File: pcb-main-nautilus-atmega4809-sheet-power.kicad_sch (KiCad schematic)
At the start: 14 parts, among them U1 NCP1117-5.0_TO252, U2 AP2112K-3.3

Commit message: Switch to generated Digi-Key and Mouser links
Supports #2.
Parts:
- C1: Digi-Key https://www.digikey.com/en/products/detail/panasonic-electr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 -> (none); Digi-Key Part Number (none) -> PCE3753CT-ND; Mouser https://www.mouser.com/ProductDetail/Panasonic/EEE-HC1E470X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 -> (none); Mouser Part Number (none) -> 667-EEE-HC1E470XP
- C2: Digi-Key https://www.digikey.com/en/products/detail/kemet/C0603C104M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 -> (none); Digi-Key Part Number (none) -> 399-C0603C104M3RAC7867CT-ND; Mouser https://www.mouser.com/ProductDetail/KEMET/C0603C104M3RAC?q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 -> (none); Mouser Part Number (none) -> 80-C0603C104M3RAC
- C3: Digi-Key https://www.digikey.com/en/products/detail/panasonic-electr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 -> (none); Digi-Key Part Number (none) -> 10-EEE-FN1A470URCT-ND; Mouser https://www.mouser.com/ProductDetail/Panasonic/EEE-FN1A470U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 -> (none); Mouser Part Number (none) -> 667-EEE-FN1A470UR
- C4, C6: Digi-Key https://www.digikey.com/en/products/detail/kemet/C0603C104M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 -> (none); Digi-Key Part Number (none) -> 399-C0603C104M8RAC7867CT-ND; Mouser https://www.mouser.com/ProductDetail/KEMET/C0603C104M8RACTU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 -> (none); Mouser Part Number (none) -> 80-C0603C104M8R
- C5: Digi-Key https://www.digikey.com/en/products/detail/kemet/C0603C106M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 -> (none); Digi-Key Part Number (none) -> 399-C0603C106M9PAC7867CT-ND; Mouser https://www.mouser.com/ProductDetail/KEMET/C0603C106M9PAC?q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 -> (none); Mouser Part Number (none) -> 80-C0603C106M9PAC
- D1, D2: Digi-Key https://www.digikey.com/en/products/detail/onsemi/MBR120LSF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 -> (none); Digi-Key Part Number (none) -> MBR120LSFT3GOSCT-ND; Mouser https://www.mouser.com/ProductDetail/onsemi/MBR120LSFT3G?qs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 -> (none); Mouser Part Number (none) -> 863-MBR120LSFT3G
- D3, D4: Digi-Key https://www.digikey.com/en/products/detail/liteon/LTST-C190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 -> (none); Digi-Key Part Number (none) -> 160-1435-1-ND; Mouser https://www.mouser.com/ProductDetail/Lite-On/LTST-C190KGKT?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 -> (none); Mouser Part Number (none) -> 859-LTST-C190KGKT
- R1, R2: Digi-Key https://www.digikey.com/en/products/detail/panasonic-electr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 -> (none); Digi-Key Part Number (none) -> P330HCT-ND; Mouser https://www.mouser.com/ProductDetail/Panasonic/ERJ-3EKF3300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 -> (none); Mouser Part Number (none) -> 667-ERJ-3EKF3300V
- U1: Digi-Key https://www.digikey.com/en/products/detail/onsemi/NCP1117DT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 -> (none); Digi-Key Part Number (none) -> NCP1117DT50RKGOSCT-ND; Mouser https://www.mouser.com/ProductDetail/onsemi/NCP1117DT50RKG?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 -> (none); Mouser Part Number (none) -> 863-NCP1117DT50RKG
- U2: Digi-Key https://www.digikey.com/en/products/detail/diodes-incorpora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 -> (none); Digi-Key Part Number (none) -> AP2112K-3.3TRG1DICT-ND; Mouser https://www.mouser.com/ProductDetail/Diodes-Incorporated/AP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 -> (none); Mouser Part Number (none) -> 621-AP2112K-3.3TRG1
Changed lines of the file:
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@@
       (effects (font (size 1.27 1.27)) hide)
     )
-    (property "Digi-Key" "https://www.digikey.com/en/products/detail/liteon/LTST-C190KGKT/386815" (id 6) (at 196.85 74.93 90)
-      (effects (font (size 1.27 1.27)) hide)
-    )
-    (property "Mouser" "https://www.mouser.com/ProductDetail/Lite-On/LTST-C190KGKT?qs=205qCy6M2Q%252BAdcgwUZktqw%3D%3D" (id 7) (at 196.85 74.93 90)
+    (property "Digi-Key Part Number" "160-1435-1-ND" (id 6) (at 196.85 74.93 90)
+      (effects (font (size 1.27 1.27)) hide)
+    )
+    (property "Mouser Part Number" "859-LTST-C190KGKT" (id 7) (at 196.85 74.93 90)
       (effects (font (size 1.27 1.27)) hide)
     )
@@
       (effects (font (size 1.27 1.27)) hide)
     )
-    (property "Digi-Key" "https://www.digikey.com/en/products/detail/panasonic-electronic-components/ERJ-3EKF3300V/1746374" (id 6) (at 196.85 85.09 0)
-      (effects (font (size 1.27 1.27)) hide)
-    )
-    (property "Mouser" "https://www.mouser.com/ProductDetail/Panasonic/ERJ-3EKF3300V?qs=MVjVSMjNRMqskx0rzM4%2FYg%3D%3D" (id 7) (at 196.85 85.09 0)
+    (property "Digi-Key Part Number" "P330HCT-ND" (id 6) (at 196.85 85.09 0)
+      (effects (font (size 1.27 1.27)) hide)
+    )
+    (property "Mouser Part Number" "667-ERJ-3EKF3300V" (id 7) (at 196.85 85.09 0)
       (effects (font (size 1.27 1.27)) hide)
     )
@@
       (effects (font (size 1.27 1.27)) hide)
     )
-    (property "Digi-Key" "https://www.digikey.com/en/products/detail/kemet/C0603C104M8RAC7867/2199783" (id 6) (at 177.8 135.89 0)
-      (effects (font (size 1.27 1.27)) hide)
-    )
-    (property "Mouser" "https://www.mouser.com/ProductDetail/KEMET/C0603C104M8RACTU?qs=t9q%2F2xDdjt%252BO6KYorkYlEw%3D%3D" (id 7) (at 177.8 135.89 0)
+    (property "Digi-Key Part Number" "399-C0603C104M8RAC7867CT-ND" (id 6) (at 177.8 135.89 0)
+      (effects (font (size 1.27 1.27)) hide)
+    )
+    (property "Mouser Part Number" "80-C0603C104M8R" (id 7) (at 177.8 135.89 0)
       (effects (font (size 1.27 1.27)) hide)
     )
@@
       (effects (font (size 1.27 1.27)) hide)
     )
-    (property "Digi-Key" "https://www.digikey.com/en/products/detail/onsemi/NCP1117DT50RKG/661206" (id 6) (at 139.7 69.85 0)
-      (effects (font (size 1.27 1.27)) hide)
-    )
-    (property "Mouser" "https://www.mouser.com/ProductDetail/onsemi/NCP1117DT50RKG?qs=Gev%252BmEvV0iaGLyZQ1w6kFw%3D%3D" (id 7) (at 139.7 69.85 0)
+    (property "Digi-Key Part Number" "NCP1117DT50RKGOSCT-ND" (id 6) (at 139.7 69.85 0)
+      (effects (font (size 1.27 1.27)) hide)
+    )
+    (property "Mouser Part Number" "863-NCP1117DT50RKG" (id 7) (at 139.7 69.85 0)
       (effects (font (size 1.27 1.27)) hide)
     )
@@
       (effects (font (size 1.27 1.27)) hide)
     )
-    (property "Digi-Key" "https://www.digikey.com/en/products/detail/panasonic-electronic-components/EEE-HC1E470XP/672769" (id 6) (at 101.6 74.93 0)
-      (effects (font (size 1.27 1.27)) hide)
-    )
-    (property "Mouser" "https://www.mouser.com/ProductDetail/Panasonic/EEE-HC1E470XP?qs=Ywefl8B65e6qyZdKUyDlkQ%3D%3D" (id 7) (at 101.6 74.93 0)
+    (property "Digi-Key Part Number" "PCE3753CT-ND" (id 6) (at 101.6 74.93 0)
+      (effects (font (size 1.27 1.27)) hide)
+    )
+    (property "Mouser Part Number" "667-EEE-HC1E470XP" (id 7) (at 101.6 74.93 0)
       (effects (font (size 1.27 1.27)) hide)
     )
@@
       (effects (font (size 1.27 1.27)) hide)
     )
-    (property "Digi-Key" "https://www.digikey.com/en/products/detail/onsemi/MBR120LSFT3G/1477155" (id 6) (at 82.55 64.77 0)
-      (effects (font (size 1.27 1.27)) hide)
-    )
-    (property "Mouser" "https://www.mouser.com/ProductDetail/onsemi/MBR120LSFT3G?qs=3JMERSakebrl0QzFyBgvHg%3D%3D" (id 7) (at 82.55 64.77 0)
+    (property "Digi-Key Part Number" "MBR120LSFT3GOSCT-ND" (id 6) (at 82.55 64.77 0)
+      (effects (font (size 1.27 1.27)) hide)
+    )
+    (property "Mouser Part Number" "863-MBR120LSFT3G" (id 7) (at 82.55 64.77 0)
       (effects (font (size 1.27 1.27)) hide)
     )
@@
       (effects (font (size 1.27 1.27)) hide)
     )
-    (property "Digi-Key" "https://www.digikey.com/en/products/detail/panasonic-electronic-components/EEE-FN1A470UR/11656979" (id 6) (at 158.75 74.93 0)
-      (effects (font (size 1.27 1.27)) hide)
-    )
-    (property "Mouser" "https://www.mouser.com/ProductDetail/Panasonic/EEE-FN1A470UR?qs=OlC7AqGiEDlZjloUmme03Q%3D%3D" (id 7) (at 158.75 74.93 0)
+    (property "Digi-Key Part Number" "10-EEE-FN1A470URCT-ND" (id 6) (at 158.75 74.93 0)
+      (effects (font (size 1.27 1.27)) hide)
+    )
+    (property "Mouser Part Number" "667-EEE-FN1A470UR" (id 7) (at 158.75 74.93 0)
       (effects (font (size 1.27 1.27)) hide)
     )
@@
       (effects (font (size 1.27 1.27)) hide)
     )
-    (property "Digi-Key" "https://www.digikey.com/en/products/detail/kemet/C0603C104M8RAC7867/2199783" (id 6) (at 177.8 74.93 0)
-      (effects (font (size 1.27 1.27)) hide)
-    )
-    (property "Mouser" "https://www.mouser.com/ProductDetail/KEMET/C0603C104M8RACTU?qs=t9q%2F2xDdjt%252BO6KYorkYlEw%3D%3D" (id 7) (at 177.8 74.93 0)
+    (property "Digi-Key Part Number" "399-C0603C104M8RAC7867CT-ND" (id 6) (at 177.8 74.93 0)
+      (effects (font (size 1.27 1.27)) hide)
+    )
+    (property "Mouser Part Number" "80-C0603C104M8R" (id 7) (at 177.8 74.93 0)
       (effects (font (size 1.27 1.27)) hide)
     )
@@
       (effects (font (size 1.27 1.27)) hide)
     )
-    (property "Digi-Key" "https://www.digikey.com/en/products/detail/liteon/LTST-C190KGKT/386815" (id 6) (at 196.85 135.89 90)
-      (effects (font (size 1.27 1.27)) hide)
-    )
-    (property "Mouser" "https://www.mouser.com/ProductDetail/Lite-On/LTST-C190KGKT?qs=205qCy6M2Q%252BAdcgwUZktqw%3D%3D" (id 7) (at 196.85 135.89 90)
+    (property "Digi-Key Part Number" "160-1435-1-ND" (id 6) (at 196.85 135.89 90)
+      (effects (font (size 1.27 1.27)) hide)
+    )
+    (property "Mouser Part Number" "859-LTST-C190KGKT" (id 7) (at 196.85 135.89 90)
       (effects (font (size 1.27 1.27)) hide)
     )
@@
       (effects (font (size 1.27 1.27)) hide)
     )
-    (property "Digi-Key" "https://www.digikey.com/en/products/detail/kemet/C0603C104M3RAC7867/416046" (id 6) (at 120.65 74.93 0)
-      (effects (font (size 1.27 1.27)) hide)
-    )
-    (property "Mouser" "https://www.mouser.com/ProductDetail/KEMET/C0603C104M3RAC?qs=zlI8QACJnq99iivvUDrLjA%3D%3D" (id 7) (at 120.65 74.93 0)
+    (property "Digi-Key Part Number" "399-C0603C104M3RAC7867CT-ND" (id 6) (at 120.65 74.93 0)
+      (effects (font (size 1.27 1.27)) hide)
+    )
+    (property "Mouser Part Number" "80-C0603C104M3RAC" (id 7) (at 120.65 74.93 0)
       (effects (font (size 1.27 1.27)) hide)
     )
@@
       (effects (font (size 1.27 1.27)) hide)
     )
-    (property "Digi-Key" "https://www.digikey.com/en/products/detail/onsemi/MBR120LSFT3G/1477155" (id 6) (at 153.67 64.77 0)
-      (effects (font (size 1.27 1.27)) hide)
-    )
-    (property "Mouser" "https://www.mouser.com/ProductDetail/onsemi/MBR120LSFT3G?qs=3JMERSakebrl0QzFyBgvHg%3D%3D" (id 7) (at 153.67 64.77 0)
+    (property "Digi-Key Part Number" "MBR120LSFT3GOSCT-ND" (id 6) (at 153.67 64.77 0)
+      (effects (font (size 1.27 1.27)) hide)
+    )
+    (property "Mouser Part Number" "863-MBR120LSFT3G" (id 7) (at 153.67 64.77 0)
       (effects (font (size 1.27 1.27)) hide)
     )
@@
       (effects (font (size 1.27 1.27)) hide)
     )
-    (property "Digi-Key" "https://www.digikey.com/en/products/detail/panasonic-electronic-components/ERJ-3EKF3300V/1746374" (id 6) (at 196.85 146.05 0)
-      (effects (font (size 1.27 1.27)) hide)
-    )
-    (property "Mouser" "https://www.mouser.com/ProductDetail/Panasonic/ERJ-3EKF3300V?qs=MVjVSMjNRMqskx0rzM4%2FYg%3D%3D" (id 7) (at 196.85 146.05 0)
+    (property "Digi-Key Part Number" "P330HCT-ND" (id 6) (at 196.85 146.05 0)
+      (effects (font (size 1.27 1.27)) hide)
+    )
+    (property "Mouser Part Number" "667-ERJ-3EKF3300V" (id 7) (at 196.85 146.05 0)
       (effects (font (size 1.27 1.27)) hide)
     )
@@
       (effects (font (size 1.27 1.27)) hide)
     )
-    (property "Digi-Key" "https://www.digikey.com/en/products/detail/kemet/C0603C106M9PAC7867/1950664" (id 6) (at 158.75 135.89 0)
-      (effects (font (size 1.27 1.27)) hide)
-    )
-    (property "Mouser" "https://www.mouser.com/ProductDetail/KEMET/C0603C106M9PAC?qs=vnwGVgFuQibgQzzOtLArWQ%3D%3D" (id 7) (at 158.75 135.89 0)
+    (property "Digi-Key Part Number" "399-C0603C106M9PAC7867CT-ND" (id 6) (at 158.75 135.89 0)
+      (effects (font (size 1.27 1.27)) hide)
+    )
+    (property "Mouser Part Number" "80-C0603C106M9PAC" (id 7) (at 158.75 135.89 0)
       (effects (font (size 1.27 1.27)) hide)
     )
@@
       (effects (font (size 1.27 1.27)) hide)
     )
-    (property "Digi-Key" "https://www.digikey.com/en/products/detail/diodes-incorporated/AP2112K-3-3TRG1/4470746" (id 6) (at 139.7 133.35 0)
-      (effects (font (size 1.27 1.27)) hide)
-    )
-    (property "Mouser" "https://www.mouser.com/ProductDetail/Diodes-Incorporated/AP2112K-3.3TRG1?qs=x6A8l6qLYDDPYHosCdzh%2FA%3D%3D" (id 7) (at 139.7 133.35 0)
-      (effects (font (size 1.27 1.27)) hide)
-    )
+    (property "Digi-Key Part Number" "AP2112K-3.3TRG1DICT-ND" (id 6) (at 139.7 133.35 0)
+      (effects (font (size 1.27 1.27)) hide)
+    )
+    (property "Mouser Part Number" "621-AP2112K-3.3TRG1" (id 7) (at 139.7 133.35 0)
+      (effects (font (size 1.27 1.27)) hide)
+    )

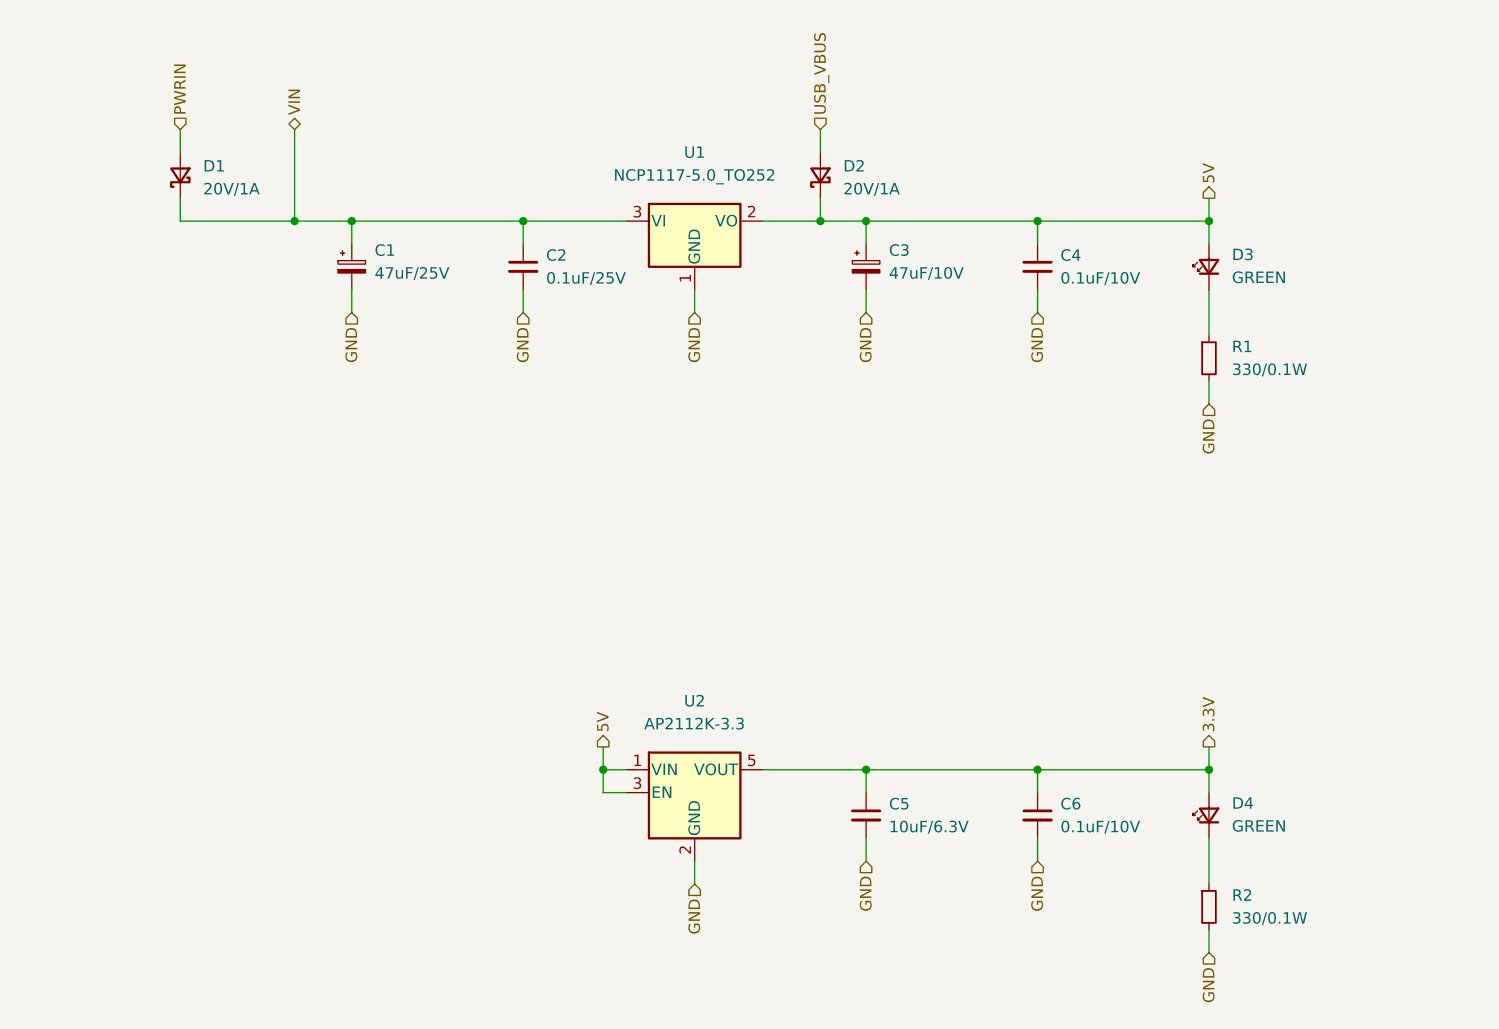
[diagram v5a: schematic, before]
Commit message: Connect root sheet
Supports #2.
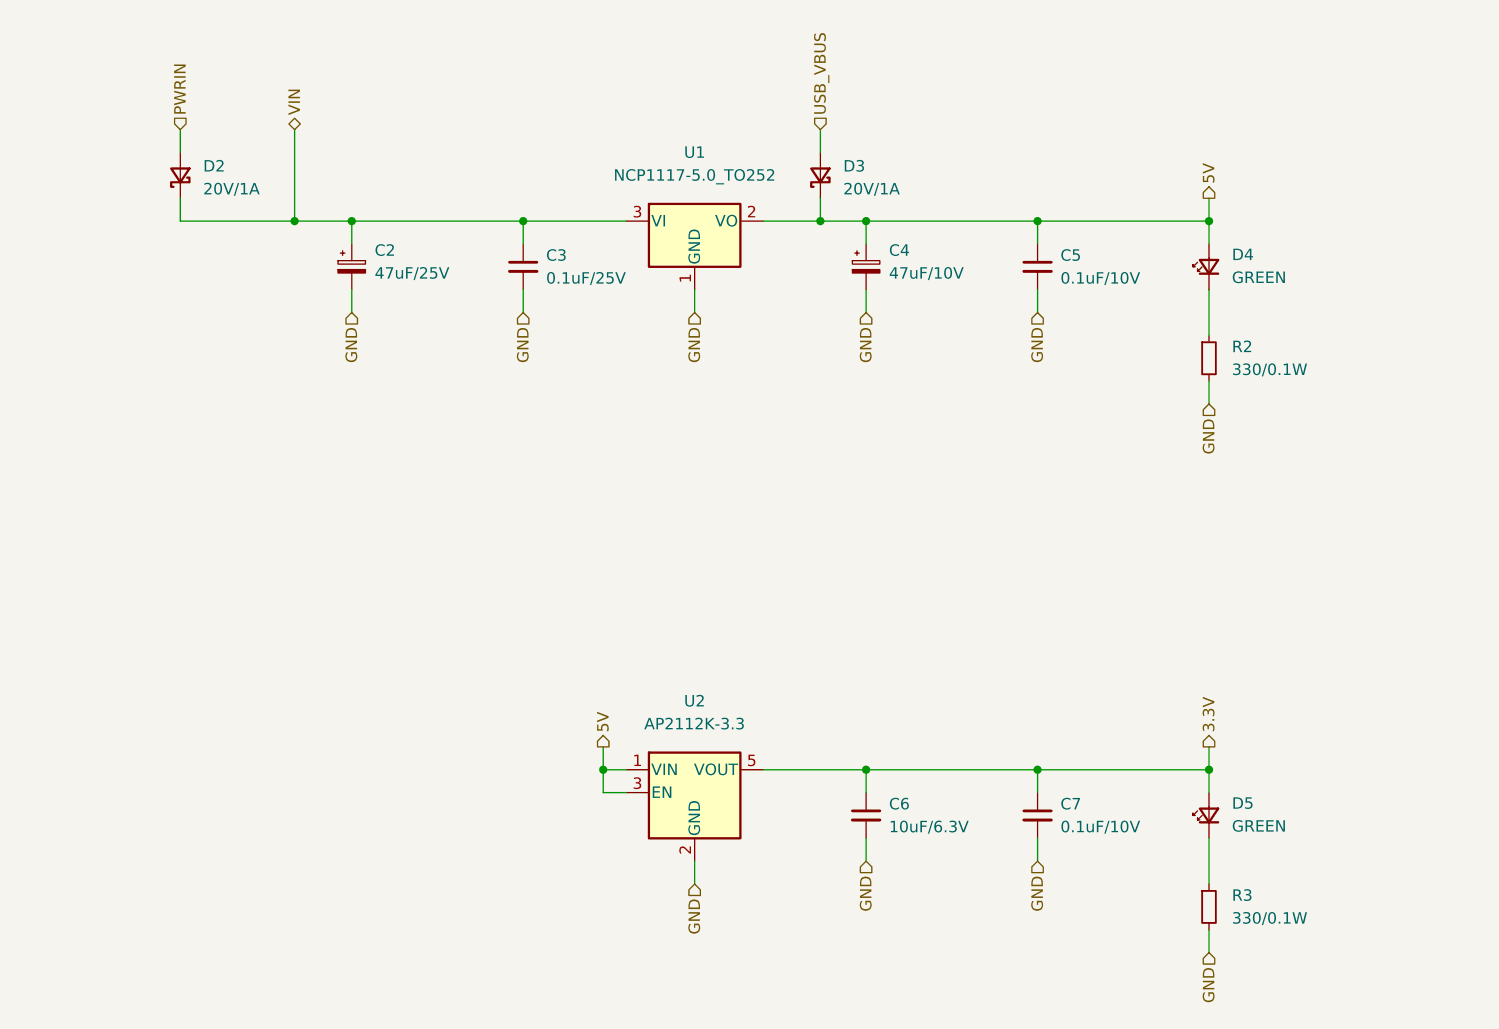
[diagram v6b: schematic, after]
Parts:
- renumbered C1 to C2, C2 to C3, C3 to C4, C4 to C5, C5 to C6, C6 to C7, D1 to D2, D2 to D3, D3 to D4, D4 to D5, R1 to R2, R2 to R3
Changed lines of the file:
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@@
   (symbol (lib_id "Device:LED_Small") (at 196.85 74.93 90) (unit 1)
     (in_bom yes) (on_board yes) (fields_autoplaced)
-    (property "Reference" "D3" (id 0) (at 199.39 73.5964 90)
+    (property "Reference" "D4" (id 0) (at 199.39 73.5964 90)
       (effects (font (size 1.27 1.27)) (justify right))
     )
@@
   (symbol (lib_id "Device:R_Small") (at 196.85 85.09 0) (unit 1)
     (in_bom yes) (on_board yes) (fields_autoplaced)
-    (property "Reference" "R1" (id 0) (at 199.39 83.8199 0)
+    (property "Reference" "R2" (id 0) (at 199.39 83.8199 0)
       (effects (font (size 1.27 1.27)) (justify left))
     )
@@
   (symbol (lib_id "Device:C_Small") (at 177.8 135.89 0) (unit 1)
     (in_bom yes) (on_board yes) (fields_autoplaced)
-    (property "Reference" "C6" (id 0) (at 180.34 134.6262 0)
+    (property "Reference" "C7" (id 0) (at 180.34 134.6262 0)
       (effects (font (size 1.27 1.27)) (justify left))
     )
@@
   (symbol (lib_id "Device:C_Polarized_Small") (at 101.6 74.93 0) (unit 1)
     (in_bom yes) (on_board yes) (fields_autoplaced)
-    (property "Reference" "C1" (id 0) (at 104.14 73.1138 0)
+    (property "Reference" "C2" (id 0) (at 104.14 73.1138 0)
       (effects (font (size 1.27 1.27)) (justify left))
     )
@@
   (symbol (lib_id "Device:D_Schottky_Small") (at 82.55 64.77 90) (unit 1)
     (in_bom yes) (on_board yes) (fields_autoplaced)
-    (property "Reference" "D1" (id 0) (at 85.09 63.7539 90)
+    (property "Reference" "D2" (id 0) (at 85.09 63.7539 90)
       (effects (font (size 1.27 1.27)) (justify right))
     )
@@
   (symbol (lib_id "Device:C_Polarized_Small") (at 158.75 74.93 0) (unit 1)
     (in_bom yes) (on_board yes) (fields_autoplaced)
-    (property "Reference" "C3" (id 0) (at 161.29 73.1138 0)
+    (property "Reference" "C4" (id 0) (at 161.29 73.1138 0)
       (effects (font (size 1.27 1.27)) (justify left))
     )
@@
   (symbol (lib_id "Device:C_Small") (at 177.8 74.93 0) (unit 1)
     (in_bom yes) (on_board yes) (fields_autoplaced)
-    (property "Reference" "C4" (id 0) (at 180.34 73.6662 0)
+    (property "Reference" "C5" (id 0) (at 180.34 73.6662 0)
       (effects (font (size 1.27 1.27)) (justify left))
     )
@@
   (symbol (lib_id "Device:LED_Small") (at 196.85 135.89 90) (unit 1)
     (in_bom yes) (on_board yes) (fields_autoplaced)
-    (property "Reference" "D4" (id 0) (at 199.39 134.5564 90)
+    (property "Reference" "D5" (id 0) (at 199.39 134.5564 90)
       (effects (font (size 1.27 1.27)) (justify right))
     )
@@
   (symbol (lib_id "Device:C_Small") (at 120.65 74.93 0) (unit 1)
     (in_bom yes) (on_board yes) (fields_autoplaced)
-    (property "Reference" "C2" (id 0) (at 123.19 73.6662 0)
+    (property "Reference" "C3" (id 0) (at 123.19 73.6662 0)
       (effects (font (size 1.27 1.27)) (justify left))
     )
@@
   (symbol (lib_id "Device:D_Schottky_Small") (at 153.67 64.77 90) (unit 1)
     (in_bom yes) (on_board yes) (fields_autoplaced)
-    (property "Reference" "D2" (id 0) (at 156.21 63.7539 90)
+    (property "Reference" "D3" (id 0) (at 156.21 63.7539 90)
       (effects (font (size 1.27 1.27)) (justify right))
     )
@@
   (symbol (lib_id "Device:R_Small") (at 196.85 146.05 0) (unit 1)
     (in_bom yes) (on_board yes) (fields_autoplaced)
-    (property "Reference" "R2" (id 0) (at 199.39 144.7799 0)
+    (property "Reference" "R3" (id 0) (at 199.39 144.7799 0)
       (effects (font (size 1.27 1.27)) (justify left))
     )
@@
   (symbol (lib_id "Device:C_Small") (at 158.75 135.89 0) (unit 1)
     (in_bom yes) (on_board yes) (fields_autoplaced)
-    (property "Reference" "C5" (id 0) (at 161.29 134.6262 0)
-      (effects (font (size 1.27 1.27)) (justify left))
-    )
+    (property "Reference" "C6" (id 0) (at 161.29 134.6262 0)
+      (effects (font (size 1.27 1.27)) (justify left))
+    )
